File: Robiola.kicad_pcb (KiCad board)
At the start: 2 copper layers, 1 part, among them U1 LM2596

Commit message: adding more component
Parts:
- added BT1: Battery, diy-modules:diy-modules-BATTERY-LI-MH12210, F.Cu at (111.2, 26.8)
- added J1: Conn_01x08, Pin_Headers:Pin_Header_Straight_1x08_Pitch2.54mm, F.Cu at (109.1, 42.8)
- added J10: Conn_01x03, Pin_Headers:Pin_Header_Straight_1x03_Pitch2.54mm, F.Cu at (109.1, 67.3)
- added J2: Conn_01x08, Pin_Headers:Pin_Header_Straight_1x08_Pitch2.54mm, F.Cu at (118.7, 42.8)
- added J3: Conn_01x08, Pin_Headers:Pin_Header_Straight_1x08_Pitch2.54mm, F.Cu at (128.4, 42.8)
- added J4: Conn_02x08_Counter_Clockwise, Pin_Headers:Pin_Header_Straight_2x08_Pitch2.54mm, F.Cu at (175.7, 17.5)
- added J5: Conn_01x03, Pin_Headers:Pin_Header_Straight_1x03_Pitch2.54mm, F.Cu at (169.7, 42.0)
- added J6: Conn_01x03, Pin_Headers:Pin_Header_Straight_1x03_Pitch2.54mm, F.Cu at (179.4, 42.0)
- added J7: Conn_01x03, Pin_Headers:Pin_Header_Straight_1x03_Pitch2.54mm, F.Cu at (138.0, 42.8)
- added J8: Conn_01x03, Pin_Headers:Pin_Header_Straight_1x03_Pitch2.54mm, F.Cu at (138.0, 54.6)
- added J9: Conn_01x03, Pin_Headers:Pin_Header_Straight_1x03_Pitch2.54mm, F.Cu at (138.0, 66.4)
- added U2: BP, Housings_DIP:DIP-40_W15.24mm_Socket_LongPads, F.Cu at (147.8, 17.6)
- added U3: TP4056, diy-modules:diy-modules-BATTERY-CHARGER-LI-5V, F.Cu at (91.3, 52.7)
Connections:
- U1 pad IN+: (no net) -> Net-(BT1-Pad1)
- U1 pad IN-: (no net) -> Net-(BT1-Pad2)
- U1 pad OUT+: (no net) -> Net-(J4-Pad10)
- U1 pad OUT-: (no net) -> Net-(J4-Pad1)

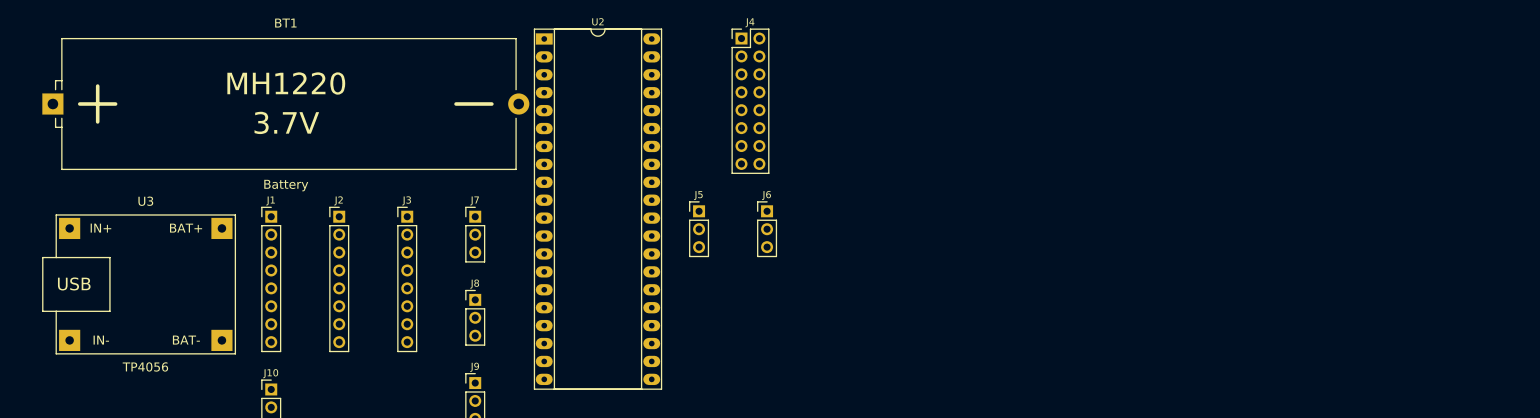
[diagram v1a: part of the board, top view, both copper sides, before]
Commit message: add desc in readme, adding some connection
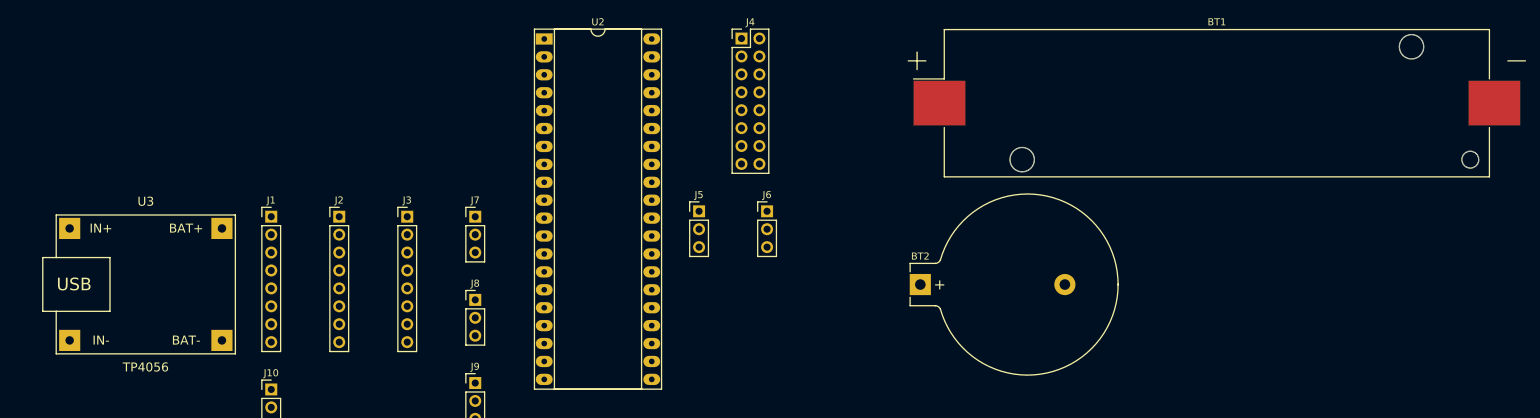
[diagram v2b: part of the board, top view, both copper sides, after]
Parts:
- added BT2: Battery_Cell, Battery_Holders:Keystone_104_1x23mm-CoinCell, F.Cu at (201.1, 52.4)
- BT1: footprint diy-modules:diy-modules-BATTERY-LI-MH12210 -> Battery_Holders:Keystone_1042_1x18650
- moved BT1 132.0 mm to (243.1, 26.7)
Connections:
- net Net-(J1-Pad6) renamed /PA5
- net Net-(J1-Pad8) renamed /PA7
- J1 pad 1: Net-(J1-Pad1) -> /PA0
- J1 pad 2: Net-(J1-Pad2) -> /PA1
- J1 pad 3: Net-(J1-Pad3) -> /PA2
- J1 pad 4: Net-(J1-Pad4) -> /PA3
- J1 pad 5: Net-(J1-Pad5) -> /PA4
- J1 pad 7: Net-(J1-Pad7) -> /PA6
- J10 pad 1: Net-(J10-Pad1) -> /PA6
- J10 pad 2: Net-(J10-Pad2) -> /+5v
- J10 pad 3: Net-(J10-Pad3) -> /GND
- J3 pad 1: Net-(J3-Pad1) -> /PB3
- J3 pad 2: Net-(J3-Pad2) -> /PB4
- J3 pad 3: Net-(J3-Pad3) -> /PB5
- J3 pad 4: Net-(J3-Pad4) -> /PB6
- J3 pad 5: Net-(J3-Pad5) -> /PB7
- J3 pad 6: Net-(J3-Pad6) -> /PB8
- J3 pad 7: Net-(J3-Pad7) -> /PB8
- J3 pad 8: Net-(J3-Pad8) -> /PB9
- J4 pad 1: Net-(J4-Pad1) -> /GND
- J4 pad 10: Net-(J4-Pad10) -> /+5v
- J4 pad 11: Net-(J4-Pad10) -> /+5v
- J4 pad 12: Net-(J4-Pad10) -> /+5v
- J4 pad 13: Net-(J4-Pad10) -> /+5v
- J4 pad 14: Net-(J4-Pad10) -> /+5v
- J4 pad 15: Net-(J4-Pad10) -> /+5v
- J4 pad 16: Net-(J4-Pad10) -> /+5v
- J4 pad 2: Net-(J4-Pad1) -> /GND
- J4 pad 3: Net-(J4-Pad1) -> /GND
- J4 pad 4: Net-(J4-Pad1) -> /GND
- J4 pad 5: Net-(J4-Pad1) -> /GND
- J4 pad 6: Net-(J4-Pad1) -> /GND
- J4 pad 7: Net-(J4-Pad1) -> /GND
- J4 pad 8: Net-(J4-Pad1) -> /GND
- J4 pad 9: Net-(J4-Pad10) -> /+5v
- J5 pad 1: Net-(J5-Pad1) -> /PA0
- J5 pad 2: Net-(J5-Pad2) -> /+5v
- J5 pad 3: Net-(J5-Pad3) -> /GND
- J6 pad 1: Net-(J6-Pad1) -> /PA1
- J6 pad 2: Net-(J6-Pad2) -> /+5v
- J6 pad 3: Net-(J6-Pad3) -> /GND
- J7 pad 1: Net-(J7-Pad1) -> /PA2
- J7 pad 2: Net-(J7-Pad2) -> /+5v
- J7 pad 3: Net-(J7-Pad3) -> /GND
- J8 pad 1: Net-(J8-Pad1) -> /PA3
- J8 pad 2: Net-(J8-Pad2) -> /+5v
- J8 pad 3: Net-(J8-Pad3) -> /GND
- J9 pad 1: Net-(J9-Pad1) -> /PA4
- J9 pad 2: Net-(J9-Pad2) -> /+5v
- J9 pad 3: Net-(J9-Pad3) -> /GND
- U1 pad OUT+: Net-(J4-Pad10) -> /+5v
- U1 pad OUT-: Net-(J4-Pad1) -> /GND
- U2 pad 18: Net-(J4-Pad10) -> /+5v
- U2 pad 19: Net-(U2-Pad19) -> /GND
- U2 pad 25: Net-(J1-Pad1) -> /PA0
- U2 pad 26: Net-(J1-Pad2) -> /PA1
- U2 pad 27: Net-(J1-Pad3) -> /PA2
- U2 pad 28: Net-(J1-Pad4) -> /PA3
- U2 pad 29: Net-(J1-Pad5) -> /PA4
- U2 pad 31: Net-(J1-Pad7) -> /PA6
- U2 pad 39: Net-(U2-Pad39) -> /GND
- U2 pad 40: Net-(U2-Pad40) -> /GND

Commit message: fixing a header, adding size estimation, add wanted feature to README
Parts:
- J4: value Conn_02x08_Counter_Clockwise -> Conn_02x08_Odd_Even
- moved BT1 135.0 mm to (111.4, 56.1)
- moved U2 77.9 mm to (117.1, 89.2), turned to 90 degrees
- moved J6 75.4 mm to (169.9, 116.8)
- moved U1 72.8 mm to (91.2, 83.3)
- moved BT2 67.1 mm to (153.0, 99.2), turned to 270 degrees
- moved J5 55.6 mm to (168.2, 97.6)
- moved J8 55.6 mm to (136.5, 110.2)
- moved J9 55.6 mm to (136.5, 122.0)
- moved J1 55.6 mm to (107.6, 98.4)
- moved J2 55.6 mm to (117.2, 98.4)
- moved J3 55.6 mm to (126.8, 98.4)
- moved J7 55.6 mm to (136.5, 98.4)
- moved U3 55.6 mm to (89.8, 108.3)
- moved J10 55.6 mm to (107.6, 122.9)
- moved J4 33.8 mm to (162.8, 48.8)
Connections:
- J4 pad 11: /+5v -> /GND
- J4 pad 13: /+5v -> /GND
- J4 pad 15: /+5v -> /GND
- J4 pad 2: /GND -> /+5v
- J4 pad 4: /GND -> /+5v
- J4 pad 6: /GND -> /+5v
- J4 pad 8: /GND -> /+5v
- J4 pad 9: /+5v -> /GND

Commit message: finishing ver 1
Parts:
- removed BT1: Battery, Battery_Holders:Keystone_1042_1x18650
- removed BT2: Battery_Cell, Battery_Holders:Keystone_104_1x23mm-CoinCell
- removed J10, J9: Conn_01x03, Pin_Headers:Pin_Header_Straight_1x03_Pitch2.54mm
- removed U3: TP4056, diy-modules:diy-modules-BATTERY-CHARGER-LI-5V
- added D1: LED, LEDs:LED_D3.0mm, F.Cu at (109.7, 74.4)
- added J11: Conn_02x02_Odd_Even, Pin_Headers:Pin_Header_Straight_2x02_Pitch2.54mm, F.Cu at (112.3, 106.9)
- added J12: Conn_02x02_Odd_Even, Pin_Headers:Pin_Header_Straight_2x02_Pitch2.54mm, F.Cu at (122.2, 44.5)
- added R1: 330, Resistors_THT:R_Axial_DIN0204_L3.6mm_D1.6mm_P5.08mm_Horizontal, F.Cu at (118.0, 74.4)
- added REF**: 1pin, Connectors:1pin, F.Cu at (122.6, 76.8)
- added REF**: 1pin, Connectors:1pin, F.Cu at (155.6, 89.5)
- added REF**: 1pin, Connectors:1pin, F.Cu at (109.0, 42.5)
- added SW1: SW_DPDT_x2, Buttons_Switches_THT:SW_CuK_JS202011CQN_DPDT_Straight, F.Cu at (110.6, 80.1)
- J2: value Conn_01x08 -> Conn_01x06; footprint Pin_Headers:Pin_Header_Straight_1x08_Pitch2.54mm -> Pin_Headers:Pin_Header_Straight_1x06_Pitch2.54mm
- J5: value Conn_01x03 -> Conn_02x08_Odd_Even; footprint Pin_Headers:Pin_Header_Straight_1x03_Pitch2.54mm -> Pin_Headers:Pin_Header_Straight_2x08_Pitch2.54mm
- J6: value Conn_01x03 -> Conn_01x08; footprint Pin_Headers:Pin_Header_Straight_1x03_Pitch2.54mm -> Pin_Headers:Pin_Header_Straight_1x08_Pitch2.54mm
- J8: value Conn_01x03 -> Barrel_Jack; footprint Pin_Headers:Pin_Header_Straight_1x03_Pitch2.54mm -> Connectors:BARREL_JACK
- moved J6 86.5 mm to (112.5, 52.1)
- moved J5 64.7 mm to (109.7, 69.8), turned to 180 degrees
- moved U1 55.9 mm to (142.9, 104.5)
- moved J1 48.3 mm to (121.3, 52.1)
- moved J3 45.5 mm to (157.5, 64.8), turned to 180 degrees
- moved J2 44.3 mm to (157.5, 80.0), turned to 180 degrees
- moved U2 30.6 mm to (147.7, 90.2), turned to 180 degrees
- moved J8 23.4 mm to (118.5, 95.2)
- moved J7 19.5 mm to (125.0, 82.7)
- moved J4 3.21 mm to (160.1, 47.0)
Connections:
- J3 pad 7: /PB8 -> /PB9
- J3 pad 8: /PB9 -> /+5V
- J4 pad 10: /+5v -> /+5V
- J4 pad 12: /+5v -> /+5V
- J4 pad 14: /+5v -> /+5V
- J4 pad 16: /+5v -> /+5V
- J4 pad 2: /+5v -> /+5V
- J4 pad 4: /+5v -> /+5V
- J4 pad 6: /+5v -> /+5V
- J4 pad 8: /+5v -> /+5V
- J5 pad 1: /PA0 -> /GND
- J5 pad 2: /+5v -> /+5V
- J6 pad 1: /PA1 -> /PA0
- J6 pad 2: /+5v -> /PA1
- J6 pad 3: /GND -> /PA2
- J7 pad 1: /PA2 -> /PB10
- J7 pad 2: /+5v -> /PB11
- J8 pad 1: /PA3 -> Net-(J11-Pad1)
- J8 pad 2: /+5v -> Net-(J11-Pad3)
- J8 pad 3: /GND -> Net-(J8-Pad3)
- U1 pad IN-: Net-(BT1-Pad2) -> Net-(J11-Pad3)
- U1 pad OUT+: /+5v -> /+5V
- U2 pad 10: Net-(J2-Pad8) -> Net-(J2-Pad6)
- U2 pad 18: /+5v -> /+5V
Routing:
- net /+5V: track 0.00 -> 228.8 mm, vias 0 -> 2
- net /GND: track 0.00 -> 198.0 mm
- net Net-(J11-Pad3): track 0.00 -> 35.1 mm
- net Net-(J11-Pad1): track 0.00 -> 34.0 mm
- net Net-(SW1-Pad1): track 0.00 -> 23.6 mm
- net /PA7: track 0.00 -> 19.9 mm
- net /PA6: track 0.00 -> 19.9 mm
- net /PA5: track 0.00 -> 19.9 mm
- net /PA4: track 0.00 -> 19.9 mm
- net /PA3: track 0.00 -> 19.9 mm
- net /PA2: track 0.00 -> 19.9 mm
- net /PA1: track 0.00 -> 19.9 mm
- net /PA0: track 0.00 -> 19.9 mm
- net /PB10: track 0.00 -> 10.7 mm
- net Net-(J12-Pad2): track 0.00 -> 10.3 mm
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- added copper zone on B.Cu, net /GND
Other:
- board text added: "Robiola 20171120"
